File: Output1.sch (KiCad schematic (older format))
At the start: 24 parts, among them J13 test, J14 test, J15 test, J16 test, J17 CONN_COAXIAL, U11 FOD0721, U12 DPBW06, U13 LTC2644, U14 uA7805, U15 INA128

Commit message: 전해콘덴서 foot print 변경
전해 콘덴서 변경
Bypass 콘데서 OPAMP에 추가 하여야 함
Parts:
- C50, C51, C53: footprint Capacitors_SMD:C_1812_HandSoldering -> USER:C_1812_HandSoldering_Polar
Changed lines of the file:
@@
 F 0 "C53" H 6975 5100 50  0000 L CNN
 F 1 "10uF" H 6975 4900 50  0000 L CNN
-F 2 "Capacitors_SMD:C_1812_HandSoldering" H 6950 5000 50  0001 C CNN
+F 2 "USER:C_1812_HandSoldering_Polar" H 6950 5000 50  0001 C CNN
 F 3 "" H 6950 5000 50  0001 C CNN
 	1    6950 5000
@@
 F 0 "C51" H 5775 5100 50  0000 L CNN
 F 1 "10uF" H 5775 4900 50  0000 L CNN
-F 2 "Capacitors_SMD:C_1812_HandSoldering" H 5750 5000 50  0001 C CNN
+F 2 "USER:C_1812_HandSoldering_Polar" H 5750 5000 50  0001 C CNN
 F 3 "" H 5750 5000 50  0001 C CNN
 	1    5750 5000
@@
 F 0 "C50" H 5325 5100 50  0000 L CNN
 F 1 "10uF" H 5325 4900 50  0000 L CNN
-F 2 "Capacitors_SMD:C_1812_HandSoldering" H 5300 5000 50  0001 C CNN
+F 2 "USER:C_1812_HandSoldering_Polar" H 5300 5000 50  0001 C CNN
 F 3 "" H 5300 5000 50  0001 C CNN
 	1    5300 5000

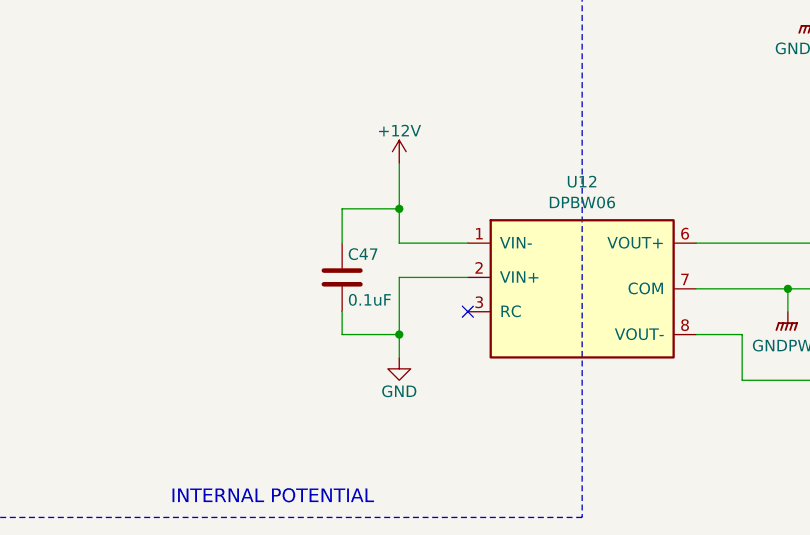
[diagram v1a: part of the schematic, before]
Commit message: 2차 PCB 1차 수정
1. ADR455 Vcc V12 수정
2. DCDC 입력전압 변경
3. Bypass 콘덴서 C66, C67 추가
4. SOIC 방향 표시
5. TLV431 PADS 변경
6. AQV258 Pin3 --> Pin2
7. 전해콘덴서 방향추가
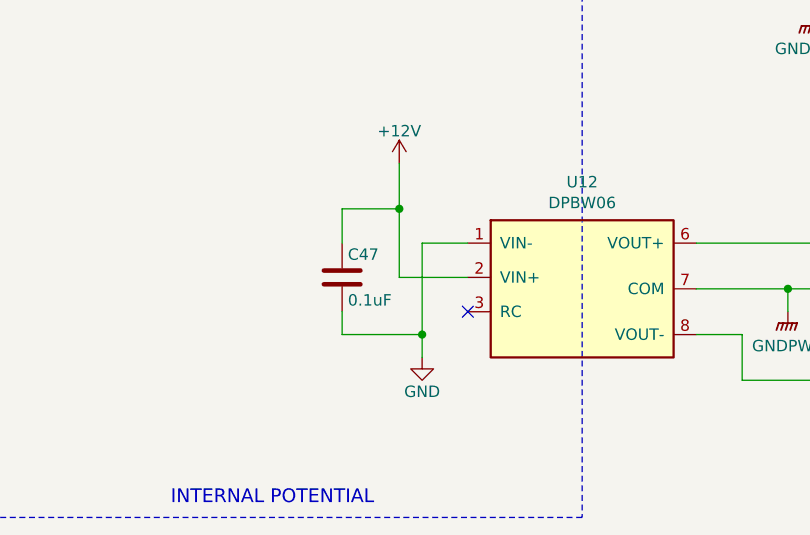
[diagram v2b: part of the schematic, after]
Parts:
- U11: footprint Housings_SOIC:SOIC-8_3.9x4.9mm_Pitch1.27mm -> USER:SOIC-8_3.9x4.9mm_Pitch1.27mm
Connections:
- net +12V: now also U12.2 (VIN+); no longer U12.1 (VIN-)
- net GND: now also U12.1 (VIN-); no longer U12.2 (VIN+)
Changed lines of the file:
@@
 F 0 "U11" H 4050 3147 60  0000 C CNN
 F 1 "FOD0721" H 4050 3041 60  0000 C CNN
-F 2 "Housings_SOIC:SOIC-8_3.9x4.9mm_Pitch1.27mm" H 4050 2750 60  0001 C CNN
+F 2 "USER:SOIC-8_3.9x4.9mm_Pitch1.27mm" H 4050 2750 60  0001 C CNN
 F 3 "" H 4050 2750 60  0001 C CNN
 	1    4050 2750
@@
 L GND #PWR087
 U 1 1 5B06E367
-P 3250 5150
-F 0 "#PWR087" H 3250 4900 50  0001 C CNN
-F 1 "GND" H 3250 5000 50  0000 C CNN
-F 2 "" H 3250 5150 50  0001 C CNN
-F 3 "" H 3250 5150 50  0001 C CNN
-	1    3250 5150
+P 3350 5150
+F 0 "#PWR087" H 3350 4900 50  0001 C CNN
+F 1 "GND" H 3350 5000 50  0000 C CNN
+F 2 "" H 3350 5150 50  0001 C CNN
+F 3 "" H 3350 5150 50  0001 C CNN
+	1    3350 5150
 	1    0    0    -1
 $EndComp
@@
 $EndComp
 Wire Wire Line
-	3250 4800 3250 5150
-Wire Wire Line
-	3250 4800 3550 4800
+	3350 4650 3350 5150
 $Comp
 L +12V #PWR086
@@
 $EndComp
 Wire Wire Line
-	3250 4300 3250 4650
-Wire Wire Line
-	3250 4650 3550 4650
+	3250 4300 3250 4800
 $Comp
 L C C47
@@
 	3000 4950 3000 5050
 Wire Wire Line
-	3000 5050 3250 5050
-Connection ~ 3250 5050
+	3000 5050 3350 5050
+Connection ~ 3350 5050
 $Comp
 L GNDPWR #PWR090
@@
 $EndComp
 Connection ~ 2650 2700
+Wire Wire Line
+	3350 4650 3550 4650
+Wire Wire Line
+	3250 4800 3550 4800
 $EndSCHEMATC

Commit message: 0805_넓히기
기타 수정
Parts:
- RV1: value 200 -> 2k
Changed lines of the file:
@@
 P 7400 2900
 F 0 "RV1" V 7500 3000 50  0000 C CNN
-F 1 "200" V 7400 2900 50  0000 C CNN
+F 1 "2k" V 7400 2900 50  0000 C CNN
 F 2 "Potentiometers:Potentiometer_Trimmer_Bourns_3296W" H 7400 2900 50  0001 C CNN
 F 3 "" H 7400 2900 50  0001 C CNN
